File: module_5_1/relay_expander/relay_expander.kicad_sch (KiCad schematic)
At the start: 46 parts, among them J1 PLS-4, J2 2EDGR-5.08-05P, J3 2EDGR-5.08-04P, J4 2EDGR-5.08-02P, J5 2EDGR-5.08-02P, K1 HF49FD/024-1H12, K2 HF49FD/024-1H12, K3 HF49FD/024-1H12, K4 HF49FD/024-1H12, K5 HF49FD/024-1H12, K6 HF49FD/024-1H12, K7 HF49FD/024-1H12, U1 STM32G030F6Px, U2 ULN2003A, U3 MP1584, U4 AMS1117-3.3, U5 MAX3078E

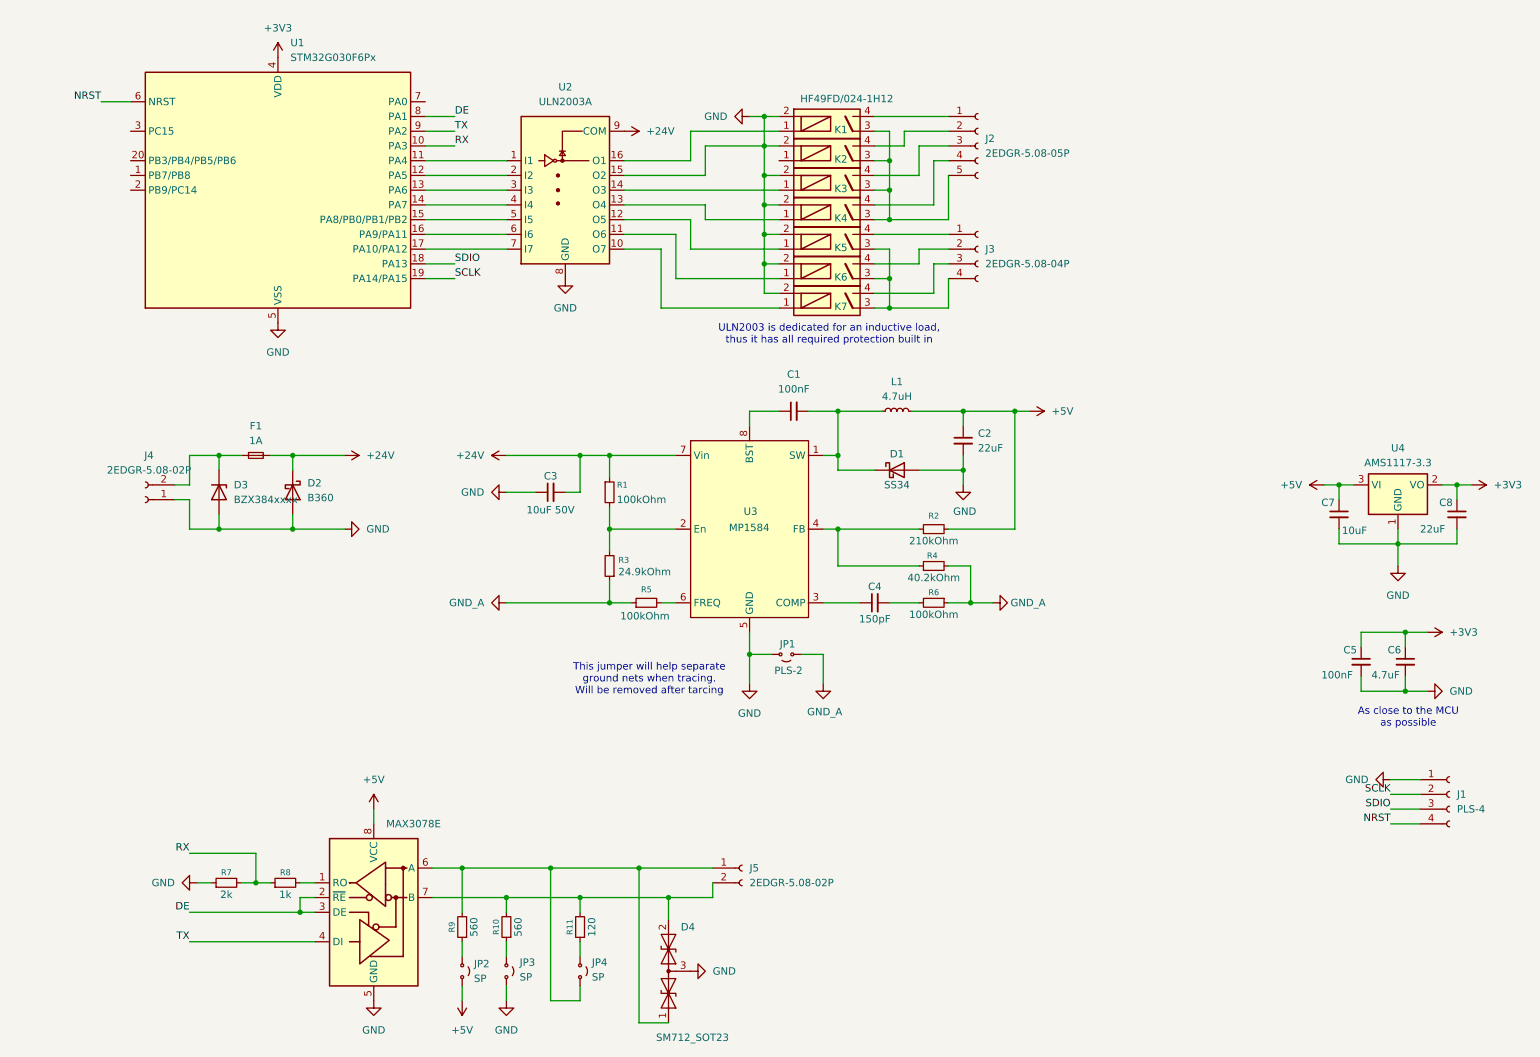
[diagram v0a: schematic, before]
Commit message: * Reverse polarity protection has been updated
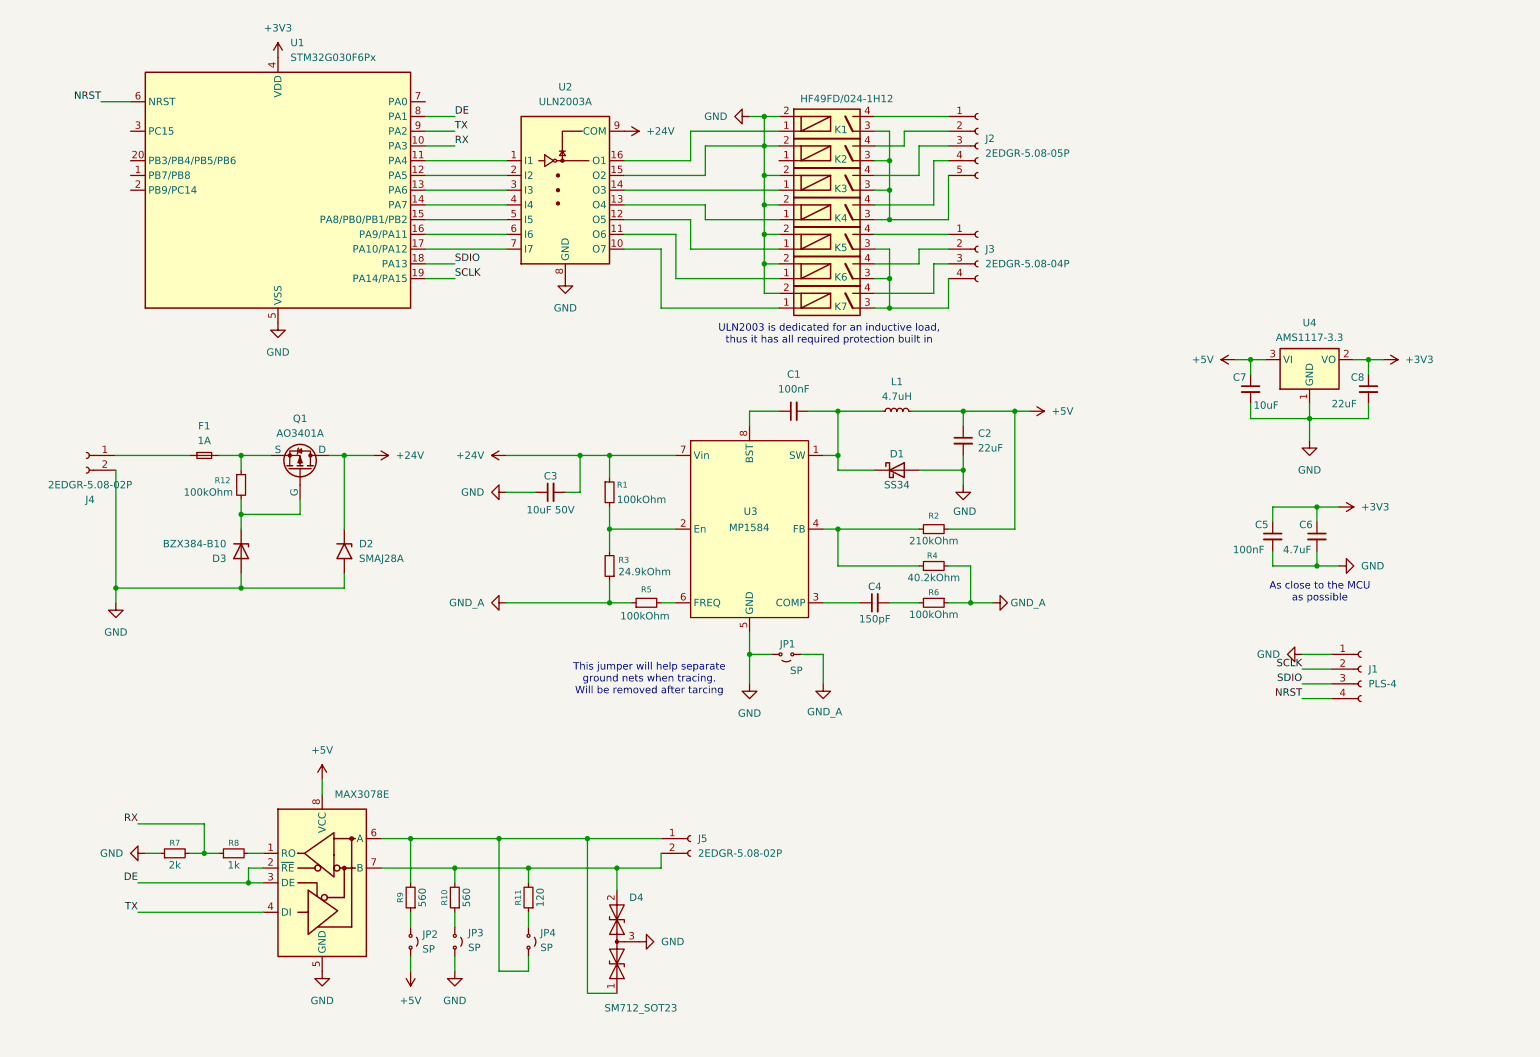
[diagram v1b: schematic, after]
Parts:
- removed D2: B360, Diode_SMD:D_SMC, symbol Diode:B360
- added D2: SMAJ28A, Diode_SMD:D_SMA, symbol Diode:SMAJ28A
- added Q1: AO3401A, Package_TO_SOT_SMD:SOT-23-3, symbol Simulation_SPICE:PMOS
- added R12: 100kOhm, Resistor_SMD:R_0201_0603Metric_Pad0.64x0.40mm_HandSolder, symbol Device:R_Small
- C2: Link (none) -> https://kosmodrom.ua/smd-kondensator-1813/chip-keramika-060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; MPM (none) -> CL10A226MQ8NRNC
- D3: value BZX384xxxx -> BZX384-B10; Link https://kosmodrom.ua/stabilitron-2/bzx384-b27-115.html -> https://kosmodrom.ua/stabilitron-2/bzx384-b10-115.html; MPM BZX384-B27.115 -> BZX384-B10.115
- J2: footprint (none) -> GMP_library:2EDGR-5.08-05P; Link (none) -> https://kosmodrom.ua/klemnik/2edgr-5-08-05p-14-00ah.html; MPM (none) -> 2EDGR-5.08-05P-14-00AH
- J3: footprint (none) -> GMP_library:2EDGR-5.08-04P; Link (none) -> https://kosmodrom.ua/klemnik/2edgr-5-08-04p-14-00ah.html; MPM (none) -> 2EDGR-5.08-04P-14-00AH
- J4, J5: footprint (none) -> GMP_library:2EDGR-5.08-02P; Link (none) -> https://kosmodrom.ua/klemnik/2edgr-5-08-02p-14-00ah.html; MPM (none) -> 2EDGR-5.08-02P-14-00AH
- JP1: value PLS-2 -> SP; now left out of the parts list
- JP2, JP3, JP4: now left out of the parts list
- L1: Link (none) -> https://kosmodrom.ua/drosel/drossel-smd0650-4-7-mkgn-2.html
- U2: Link (none) -> https://kosmodrom.ua/tranzistor-darlington/uln2003adr.html; MPM (none) -> ULN2003ADR
- U3: Link (none) -> https://kosmodrom.ua/dc-dc-peretvoryuvach-integralniy/mp158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; MPM (none) -> MP1584EN
- U4: Link (none) -> https://kosmodrom.ua/stabilizator-naprugi/ams1117-3-3.html; MPM (none) -> AMS1117-3.3
- U5: Link (none) -> https://kosmodrom.ua/interfeys-rs-422-rs-485-2/sp485ren-l-t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; MPM (none) -> SP485REN-L/TR
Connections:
- net +24V: now also D2.1 (A1), Q1.1 (D); no longer F1.2
- net GND: now also J4.2 (Pin_2), D2.2 (A2); no longer J4.1 (Pin_1)
- new net: D3.1 (K), Q1.2 (G), R12.2
- new net: F1.1, J4.1 (Pin_1)
- new net: F1.2, Q1.3 (S), R12.1
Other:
- moved on the sheet: C5, C6, C7, C8, D4, F1, J1, J4, J5, JP2, JP3, JP4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

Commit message: * Schematic almost done * First approximation of PCB is ready, but I would like to move all connectors to one side
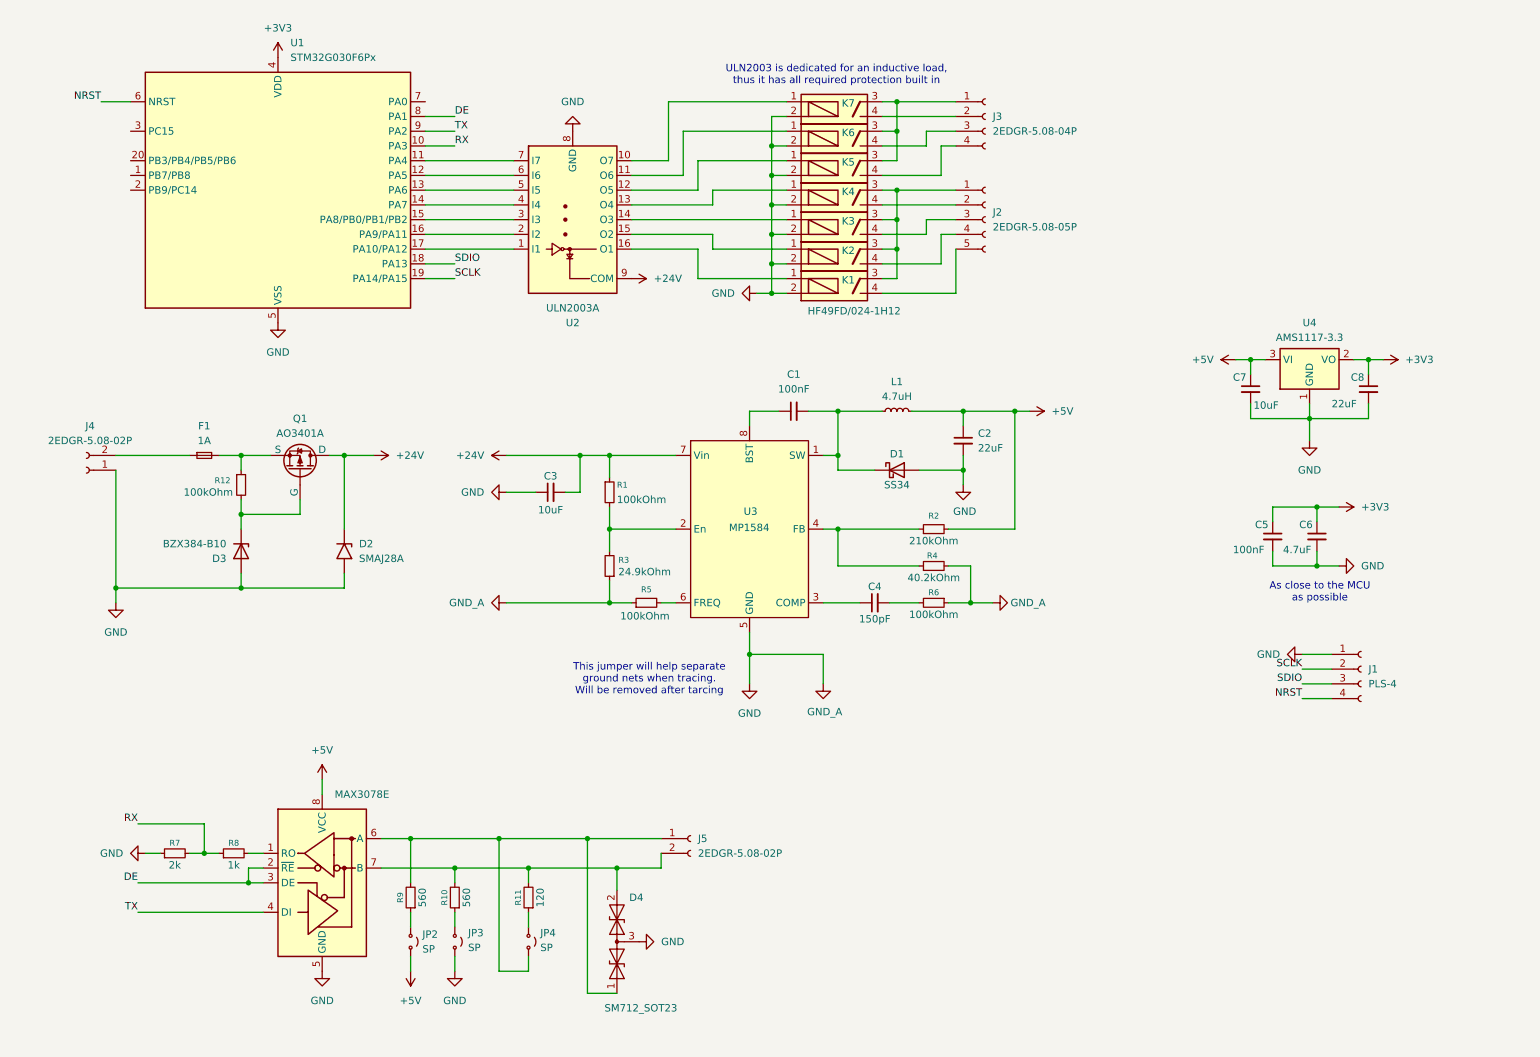
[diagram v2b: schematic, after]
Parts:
- removed JP1: SP, Jumper:SolderJumper-2_P1.3mm_Open_TrianglePad1.0x1.5mm, symbol Jumper:Jumper_2_Small_Open
- C2, C8: footprint Capacitor_SMD:C_0603_1608Metric_Pad1.08x0.95mm_HandSolder -> Capacitor_SMD:C_1206_3216Metric_Pad1.33x1.80mm_HandSolder; Link https://kosmodrom.ua/smd-kondensator-1813/chip-keramika-060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 -> https://kosmodrom.ua/smd-kondensator-1813/chip-keramika-120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; MPM CL10A226MQ8NRNC -> CL31X476KQHNNNE
- C3: value 10uF 50V -> 10uF; footprint Capacitor_SMD:C_0603_1608Metric_Pad1.08x0.95mm_HandSolder -> Capacitor_SMD:C_1206_3216Metric_Pad1.33x1.80mm_HandSolder
- C7: footprint Capacitor_SMD:C_0603_1608Metric_Pad1.08x0.95mm_HandSolder -> Capacitor_SMD:C_1206_3216Metric_Pad1.33x1.80mm_HandSolder; Link https://kosmodrom.ua/smd-kondensator-1813/chip-keramika-060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 -> https://kosmodrom.ua/smd-kondensator-1813/chip-keramika-120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
- F1: footprint (none) -> Resistor_THT:R_Axial_DIN0414_L11.9mm_D4.5mm_P15.24mm_Horizontal; Link (none) -> https://kosmodrom.ua/zapobizhnik-plavkiy/fuse-1a-250v-3x10.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; MPM (none) -> FUSE 1A 250V 3X10
- R1, R10, R11, R12, R2, R3, R4, R5, R6, R7, R8, R9: footprint Resistor_SMD:R_0201_0603Metric_Pad0.64x0.40mm_HandSolder -> Resistor_SMD:R_0603_1608Metric_Pad0.98x0.95mm_HandSolder
- U3: footprint Package_SO:SOIC-8_5.3x5.3mm_P1.27mm -> Package_SO:SOIC-8_3.9x4.9mm_P1.27mm
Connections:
- net GND_A is gone; now on net GND: R3.1, R4.2, R5.1, R6.1
- net +24V: now also Q1.3 (D); no longer Q1.1 (D)
- net GND: now also J4.1 (Pin_1); no longer J4.2 (Pin_2), U2.15 (O2)
- net at K1.3, K2.3, K3.3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: now also J2.1 (Pin_1); no longer J2.5 (Pin_5)
- net at K1.4: now also J2.5 (Pin_5); no longer J2.1 (Pin_1)
- net at K4.4: now also J2.2 (Pin_2); no longer J2.4 (Pin_4)
- net at U2.1 (I1): now also U1.17 (PA10/PA12); no longer U1.11 (PA4)
- net at U2.2 (I2): now also U1.16 (PA9/PA11); no longer U1.12 (PA5)
- net at U2.3 (I3): now also U1.15 (PA8/PB0/PB1/PB2); no longer U1.13 (PA6)
- net at U2.5 (I5): now also U1.13 (PA6); no longer U1.15 (PA8/PB0/PB1/PB2)
- net at U2.6 (I6): now also U1.12 (PA5); no longer U1.16 (PA9/PA11)
- net at U2.7 (I7): now also U1.11 (PA4); no longer U1.17 (PA10/PA12)
- net at D3.1 (K), R12.2: now also Q1.1 (G); no longer Q1.2 (G)
- net at K2.4: now also J2.4 (Pin_4); no longer J2.2 (Pin_2)
- net at K5.3, K6.3, K7.3: now also J3.1 (Pin_1); no longer J3.4 (Pin_4)
- net at K6.4: now also J3.3 (Pin_3); no longer J3.2 (Pin_2)
- net at F1.1: now also J4.2 (Pin_2); no longer J4.1 (Pin_1)
- net at K5.4: now also J3.4 (Pin_4); no longer J3.1 (Pin_1)
- net at K7.4: now also J3.2 (Pin_2); no longer J3.3 (Pin_3)
- net at F1.2, R12.1: now also Q1.2 (S); no longer Q1.3 (S)
- net at K2.1: now also U2.15 (O2)
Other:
- moved on the sheet: J2, J3, J4, K1, K2, K3, K4, K5, K6, K7, U2

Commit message: PCB has been traced. Tiny improvements: * big capacitor on power input; * power indicating LED;
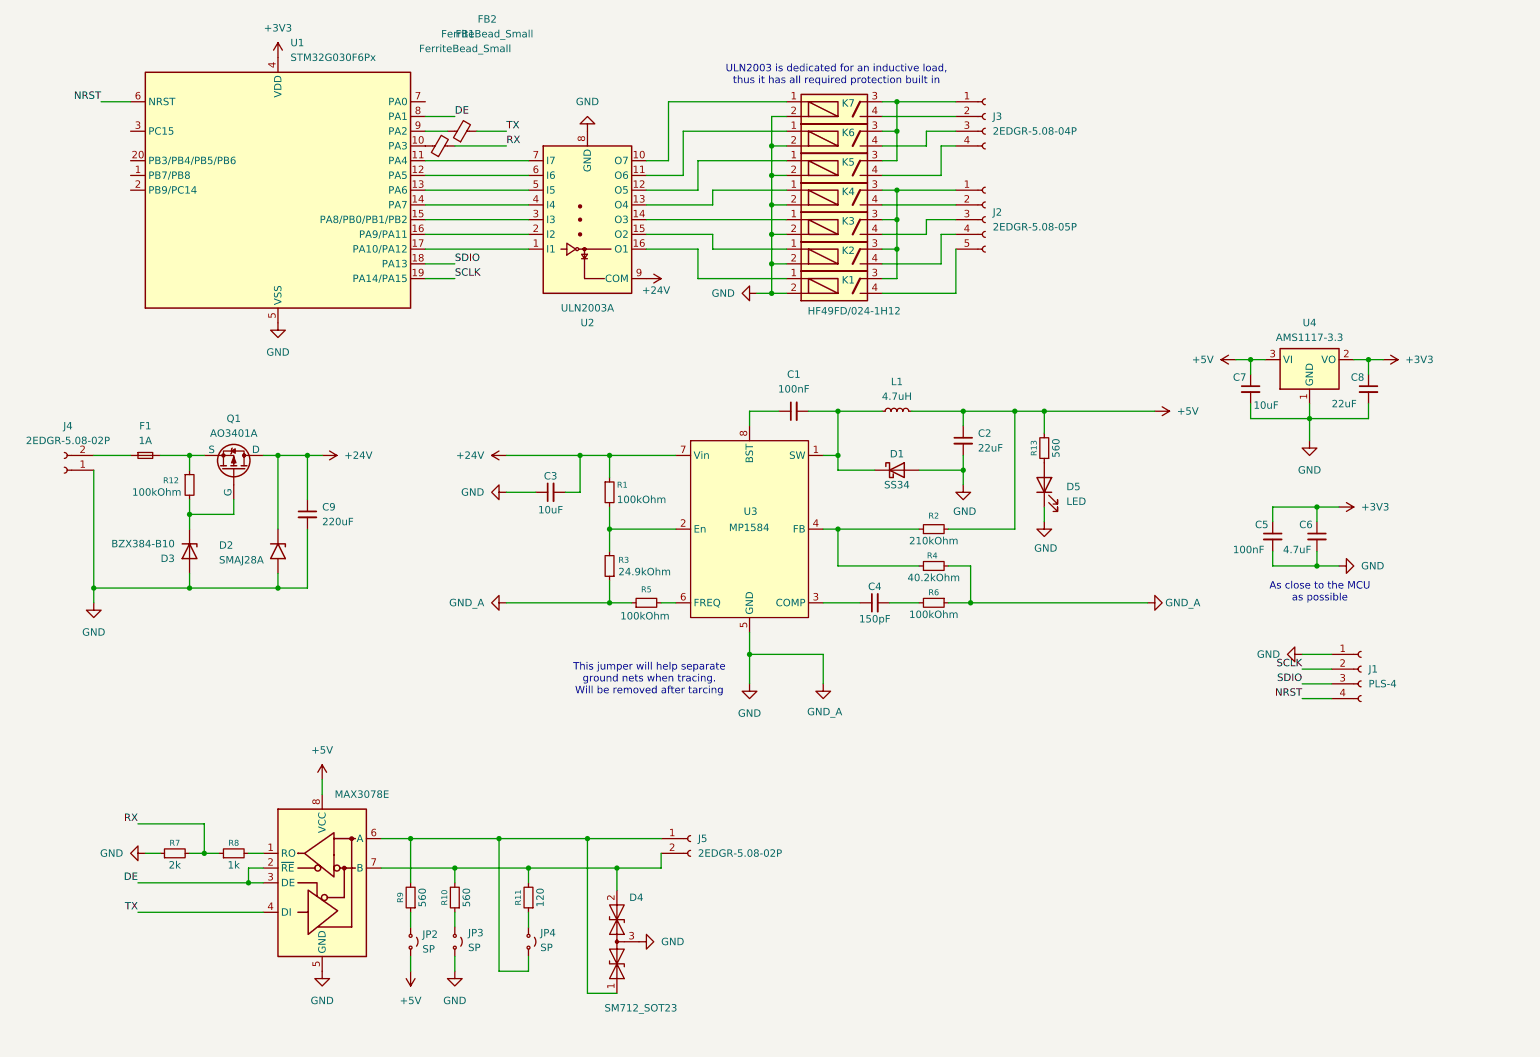
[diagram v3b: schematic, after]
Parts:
- added C9: 220uF, Capacitor_SMD:CP_Elec_8x10.5, symbol Device:C_Small
- added D5: LED, LED_SMD:LED_0805_2012Metric_Pad1.15x1.40mm_HandSolder, symbol Device:LED
- added FB1, FB2: FerriteBead_Small, Capacitor_SMD:C_0805_2012Metric_Pad1.18x1.45mm_HandSolder, symbol Device:FerriteBead_Small
- added R13: 560, Resistor_SMD:R_0603_1608Metric_Pad0.98x0.95mm_HandSolder, symbol Device:R_Small
- C4: Link (none) -> https://kosmodrom.ua/smd-kondensator-1813/c1608c0g2e151j080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; MPM (none) -> C1608C0G2E151J080AA
- C7: MPM CL10A106MP8NNNC -> CL31B106KBHNNNE
- K1, K2, K3, K4, K5, K6, K7: Link 2 (none) -> https://www.rcscomponents.kiev.ua/product/rele-hf49fd-024-1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; MPM (none) -> HF49FD/024-1H12
- R1, R12, R5, R6: Link (none) -> https://kosmodrom.ua/smd-rezistor-2513/smd-rezistor-0603-10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; MPM (none) -> RC0603FR-07100KL
- R10, R9: Link (none) -> https://www.rcscomponents.kiev.ua/product/560-ohm-5-0-1w-50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; MPM (none) -> RC03K3561JT-KOME
- R11: Link (none) -> https://kosmodrom.ua/smd-rezistor-2513/smd-rezistor-0603-12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; MPM (none) -> RC0603JR-07120RL
- R2: Link (none) -> https://www.rcscomponents.kiev.ua/product/210-kohm-1-0-125w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; MPM (none) -> RC0805FR-210K-Hitano
- R3: footprint Resistor_SMD:R_0603_1608Metric_Pad0.98x0.95mm_HandSolder -> Resistor_SMD:R_0805_2012Metric_Pad1.20x1.40mm_HandSolder; Link (none) -> https://m-teh.com.ua/rezistor-smd-24.9k-0805-1/; MPM (none) -> SMD 24.9K 0805 1%
- R4: Link (none) -> https://www.rcscomponents.kiev.ua/product/40-2-kohm-1-0-1w-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; MPM (none) -> RC0603FR-40K2R-Hitano
- R7: Link (none) -> https://kosmodrom.ua/smd-rezistor-2513/smd-rezistor-0603-2-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; MPM (none) -> RC0603FR-072KL
- R8: Link (none) -> https://kosmodrom.ua/smd-rezistor-2513/smd-rezistor-0603-1-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; MPM (none) -> RC0603FR-071KL
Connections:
- net +24V: now also C9.1
- net +5V: now also R13.2
- net GND: now also C9.2, D5.1 (K)
- net RX: now also FB1.2; no longer U1.10 (PA3)
- net TX: now also FB2.2; no longer U1.9 (PA2)
- new net: FB1.1, U1.10 (PA3)
- new net: FB2.1, U1.9 (PA2)
- new net: D5.2 (A), R13.1
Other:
- moved on the sheet: D2, D3, F1, J4, Q1, R12, U2
